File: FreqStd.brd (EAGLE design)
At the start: 50.8 x 43.2 mm, 33 parts, among them J1 ISP Connector, J2 BNC_RIGHT-ANGLE, SW1 PWR, U1 ATMEGA328, U2 MIC5205, U3 SN74LV164APW

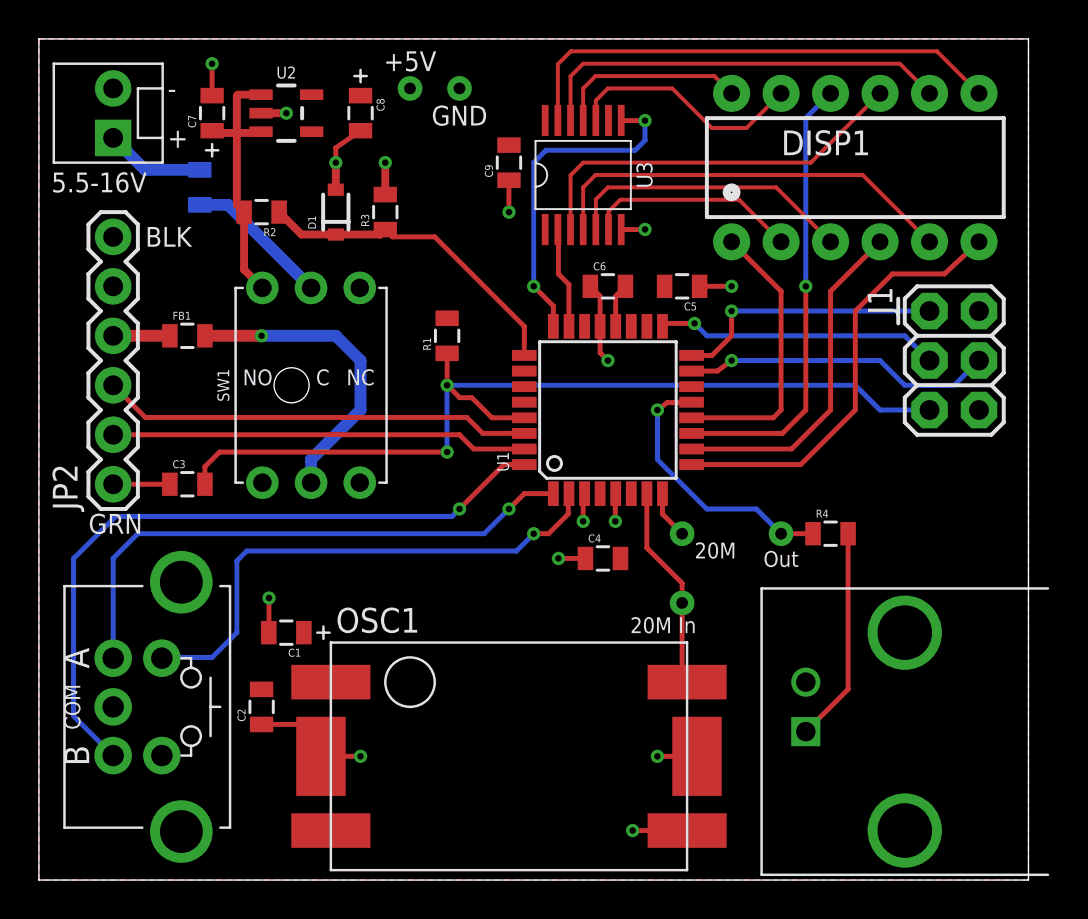
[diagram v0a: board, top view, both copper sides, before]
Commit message: Rev A board as ordered
Minor changes for ordering.  Added OSHPark renderings.  Started writing
firmware and GitHub cover.
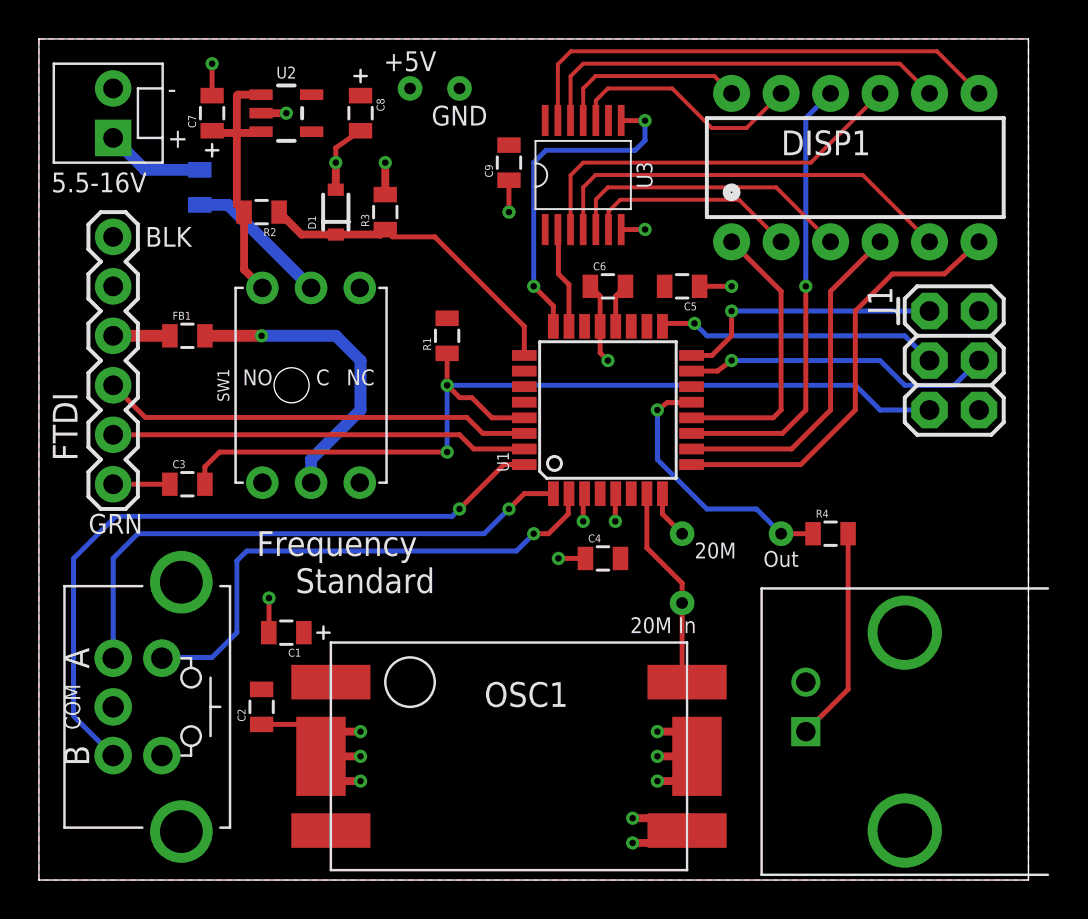
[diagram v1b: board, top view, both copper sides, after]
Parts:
- moved FRAME1 11.4 mm to (49.5, 17.8)
- renumbered JP2 to FTDI
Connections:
- net N$7 renamed SR_CLK
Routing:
- net GND: track 34.0 -> 42.7 mm, vias 15 -> 20
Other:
- board text added: "Frequency Standard"
- board text added: "http://github.com/uchip/FrequencyStandard"
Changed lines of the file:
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@@
 <?xml version="1.0" encoding="utf-8"?>
 <!DOCTYPE eagle SYSTEM "eagle.dtd">
-<eagle version="7.3.0">
+<eagle version="7.4.0">
 <drawing>
 <settings>
@@
 <layer number="49" name="Reference" color="7" fill="1" visible="no" active="yes"/>
 <layer number="50" name="dxf" color="7" fill="1" visible="no" active="no"/>
-<layer number="51" name="tDocu" color="6" fill="1" visible="yes" active="yes"/>
+<layer number="51" name="tDocu" color="6" fill="1" visible="no" active="yes"/>
 <layer number="52" name="bDocu" color="7" fill="1" visible="no" active="yes"/>
 <layer number="53" name="tGND_GNDA" color="7" fill="1" visible="no" active="no"/>
@@
 <text x="30.353" y="13.081" size="0.8128" layer="21" font="vector" ratio="15" align="center-left">20M In</text>
 <text x="33.655" y="16.51" size="0.8128" layer="21" font="vector" ratio="15">20M</text>
+<text x="11.176" y="14.732" size="1.27" layer="21" font="vector" ratio="15">Frequency
+    Standard</text>
+<text x="46.99" y="5.08" size="1.27" layer="22" font="vector" ratio="15" rot="MR45">http://github.com/uchip/FrequencyStandard</text>
 </plain>
 <attributes>
@@
 <elements>
 <element name="OSC1" library="playground" package="TCXO" value="" x="24.13" y="6.35" smashed="yes">
-<attribute name="NAME" x="15.24" y="12.7" size="1.27" layer="25" font="vector" ratio="15"/>
+<attribute name="NAME" x="22.86" y="8.89" size="1.27" layer="25" font="vector" ratio="15"/>
 <attribute name="VALUE" x="24.13" y="-1.27" size="1.27" layer="27" font="vector" ratio="15" align="bottom-center"/>
 </element>
@@
 <attribute name="VALUE" x="35.56" y="21.59" size="0.4064" layer="27" rot="R90"/>
 </element>
-<element name="JP2" library="SparkFun" package="1X06" value="FTDI Basic" x="3.81" y="20.32" smashed="yes" rot="R90">
-<attribute name="NAME" x="1.9812" y="18.9738" size="1.27" layer="25" ratio="15" rot="R90"/>
+<element name="FTDI" library="SparkFun" package="1X06" value="FTDI Basic" x="3.81" y="20.32" smashed="yes" rot="R90">
+<attribute name="NAME" x="1.9812" y="21.5138" size="1.27" layer="25" ratio="15" rot="R90"/>
 <attribute name="VALUE" x="6.985" y="19.05" size="1.27" layer="27" rot="R90"/>
 </element>
@@
 <attribute name="VALUE" x="9.652" y="36.576" size="0.4064" layer="28" rot="MR270"/>
 </element>
-<element name="FRAME1" library="NewFrame" package="FR-LTR-ON-PCB" value="FRAME_LTR_CU_MARK" x="49.53" y="6.35">
-<attribute name="CNAME" value="Frequency Standard" x="49.53" y="6.35" size="1.778" layer="27" display="off"/>
-<attribute name="CREVISION" value="Rev A" x="49.53" y="6.35" size="1.778" layer="27" display="off"/>
-<attribute name="DATECODE" value="27AUG2015" x="49.53" y="6.35" size="1.778" layer="27" display="off"/>
-<attribute name="DESIGNER" value="C.Schnarel" x="49.53" y="6.35" size="1.778" layer="27" display="off"/>
+<element name="FRAME1" library="NewFrame" package="FR-LTR-ON-PCB" value="FRAME_LTR_CU_MARK" x="49.53" y="17.78">
+<attribute name="CNAME" value="Frequency Standard" x="49.53" y="17.78" size="1.778" layer="27" display="off"/>
+<attribute name="CREVISION" value="Rev A" x="49.53" y="17.78" size="1.778" layer="27" display="off"/>
+<attribute name="DATECODE" value="02SEP2015" x="49.53" y="17.78" size="1.778" layer="27" display="off"/>
+<attribute name="DESIGNER" value="C.Schnarel" x="49.53" y="17.78" size="1.778" layer="27" display="off"/>
 </element>
 <element name="TP4" library="ChipsParts" package="BBD-VIA" value="TEST_POINT" x="33.02" y="17.78"/>
@@
 <contactref element="U1" pad="3"/>
 <contactref element="U1" pad="21"/>
-<contactref element="JP2" pad="5"/>
-<contactref element="JP2" pad="6"/>
+<contactref element="FTDI" pad="5"/>
+<contactref element="FTDI" pad="6"/>
 <contactref element="J1" pad="6"/>
 <contactref element="R3" pad="2"/>
@@
 <via x="31.75" y="6.35" extent="1-16" drill="0.3302"/>
 <via x="16.51" y="6.35" extent="1-16" drill="0.3302"/>
-<via x="30.48" y="2.54" extent="1-16" drill="0.3302"/>
+<via x="30.48" y="3.175" extent="1-16" drill="0.3302"/>
 <via x="12.7" y="39.37" extent="1-16" drill="0.3302"/>
 <via x="8.89" y="41.91" extent="1-16" drill="0.3302"/>
@@
 <wire x1="13.6" y1="7.99" x2="13.97" y2="7.62" width="0.254" layer="1"/>
 <wire x1="13.97" y1="7.62" x2="13.97" y2="6.858" width="0.254" layer="1"/>
-<wire x1="13.97" y1="6.858" x2="14.478" y2="6.35" width="0.254" layer="1"/>
-<wire x1="16.51" y1="6.35" x2="14.478" y2="6.35" width="0.254" layer="1"/>
-<wire x1="31.75" y1="6.35" x2="33.782" y2="6.35" width="0.254" layer="1"/>
-<wire x1="30.48" y1="2.54" x2="33.274" y2="2.54" width="0.254" layer="1"/>
+<wire x1="13.97" y1="6.858" x2="15.131534375" y2="7.75971875" width="0.254" layer="1"/>
+<wire x1="15.131534375" y1="7.75971875" x2="14.478" y2="6.35" width="0.254" layer="1"/>
 <via x="11.811" y="14.478" extent="1-16" drill="0.3302"/>
 <wire x1="11.8" y1="12.7" x2="11.811" y2="12.711" width="0.254" layer="1"/>
@@
 <contactref element="TP2" pad="P$1"/>
 <contactref element="S1" pad="E"/>
+<via x="16.51" y="7.62" extent="1-16" drill="0.3302"/>
+<via x="16.51" y="5.08" extent="1-16" drill="0.3302"/>
+<via x="31.75" y="7.62" extent="1-16" drill="0.3302"/>
+<via x="31.75" y="5.08" extent="1-16" drill="0.3302"/>
+<wire x1="16.51" y1="6.35" x2="15.24" y2="6.35" width="0.4064" layer="1"/>
+<wire x1="16.51" y1="7.62" x2="15.131534375" y2="7.62" width="0.4064" layer="1"/>
+<wire x1="15.131534375" y1="7.62" x2="15.131534375" y2="7.75971875" width="0.4064" layer="1"/>
+<wire x1="16.51" y1="5.08" x2="15.24" y2="5.08" width="0.4064" layer="1"/>
+<wire x1="31.75" y1="7.62" x2="33.02" y2="7.62" width="0.4064" layer="1"/>
+<wire x1="31.75" y1="6.35" x2="33.02" y2="6.35" width="0.4064" layer="1"/>
+<wire x1="31.75" y1="5.08" x2="33.02" y2="5.08" width="0.4064" layer="1"/>
+<via x="30.48" y="1.905" extent="1-16" drill="0.3302"/>
+<wire x1="30.48" y1="3.175" x2="31.75" y2="3.175" width="0.4064" layer="1"/>
+<wire x1="30.48" y1="1.905" x2="31.75" y2="1.905" width="0.4064" layer="1"/>
+<wire x1="31.75" y1="1.905" x2="31.75" y2="2.54" width="0.4064" layer="1"/>
+<wire x1="31.75" y1="2.54" x2="31.75" y2="3.175" width="0.4064" layer="1"/>
+<wire x1="31.75" y1="2.54" x2="33.274" y2="2.54" width="0.4064" layer="1"/>
+<wire x1="33.02" y1="6.35" x2="33.782" y2="6.35" width="0" layer="19" extent="1-1"/>
 </signal>
 <signal name="AREF">
@@
 <signal name="TXO">
 <contactref element="U1" pad="31"/>
-<contactref element="JP2" pad="2"/>
+<contactref element="FTDI" pad="2"/>
 <wire x1="24.9174" y1="22.13" x2="22.32" y2="22.13" width="0.254" layer="1"/>
 <wire x1="22.32" y1="22.13" x2="21.59" y2="22.86" width="0.254" layer="1"/>
@@
 </signal>
 <signal name="DTR">
-<contactref element="JP2" pad="1"/>
+<contactref element="FTDI" pad="1"/>
 <contactref element="C3" pad="1"/>
 <wire x1="6.72" y1="20.32" x2="3.81" y2="20.32" width="0.254" layer="1"/>
 </signal>
 <signal name="RXI">
-<contactref element="JP2" pad="3"/>
+<contactref element="FTDI" pad="3"/>
 <contactref element="U1" pad="30"/>
 <wire x1="24.9174" y1="22.93" x2="22.79" y2="22.93" width="0.254" layer="1"/>
@@
 <signal name="VCCUSB">
 <contactref element="FB1" pad="1"/>
-<contactref element="JP2" pad="4"/>
+<contactref element="FTDI" pad="4"/>
 <wire x1="3.81" y1="27.94" x2="6.72" y2="27.94" width="0.6096" layer="1"/>
 </signal>
@@
 <wire x1="35.941" y1="34.925" x2="38.1" y2="32.766" width="0.2032" layer="1"/>
 </signal>
-<signal name="N$7">
+<signal name="SR_CLK">
 <contactref element="U3" pad="8"/>
 <contactref element="U1" pad="24"/>
@@
 </board>
 </drawing>
+<compatibility>
+<note version="6.3" minversion="6.2.2" severity="warning">
+Since Version 6.2.2 text objects can contain more than one line,
+which will not be processed correctly with this version.
+</note>
+</compatibility>
 </eagle>
